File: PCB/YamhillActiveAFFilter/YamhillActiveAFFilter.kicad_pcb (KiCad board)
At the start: 2 copper layers, 50 x 50 mm, 32 parts, among them J1 Input, J2 +5V, J3 Output, U1 TL974

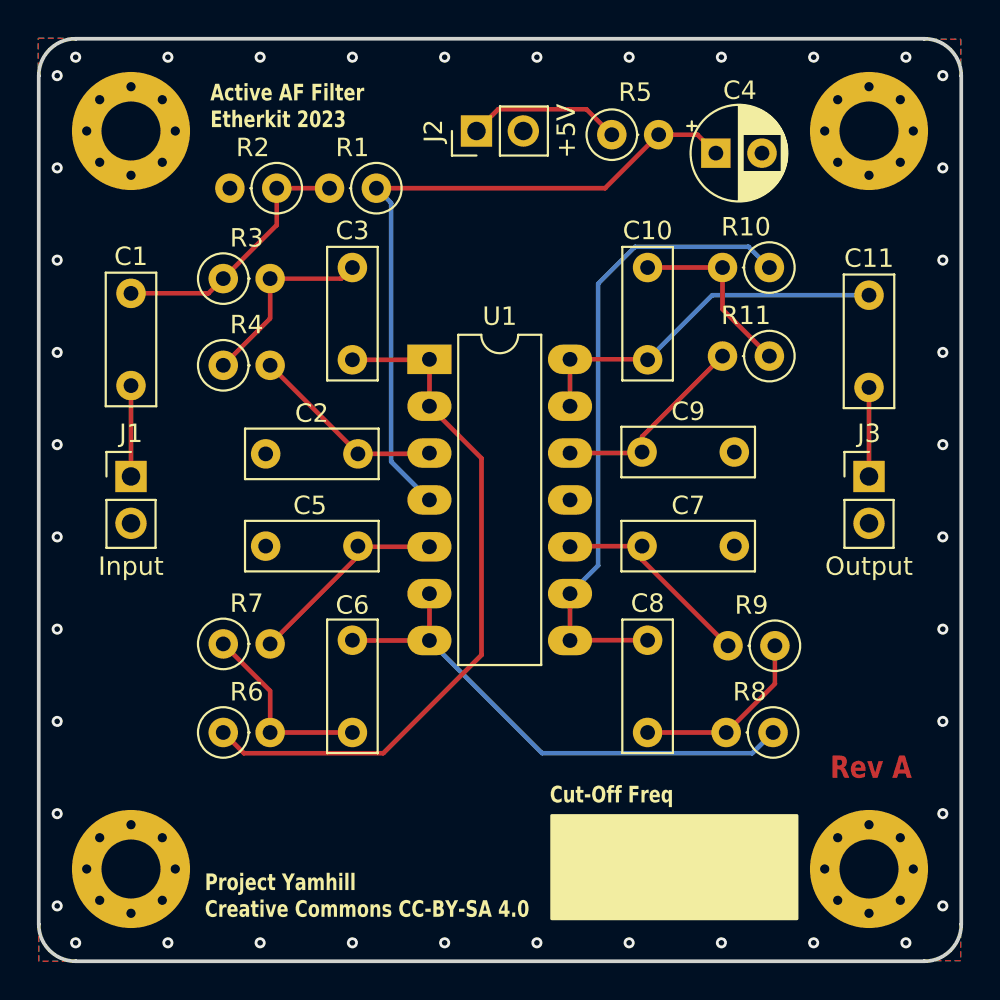
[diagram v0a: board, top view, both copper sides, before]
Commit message: AF Filter, Protoboard modules added
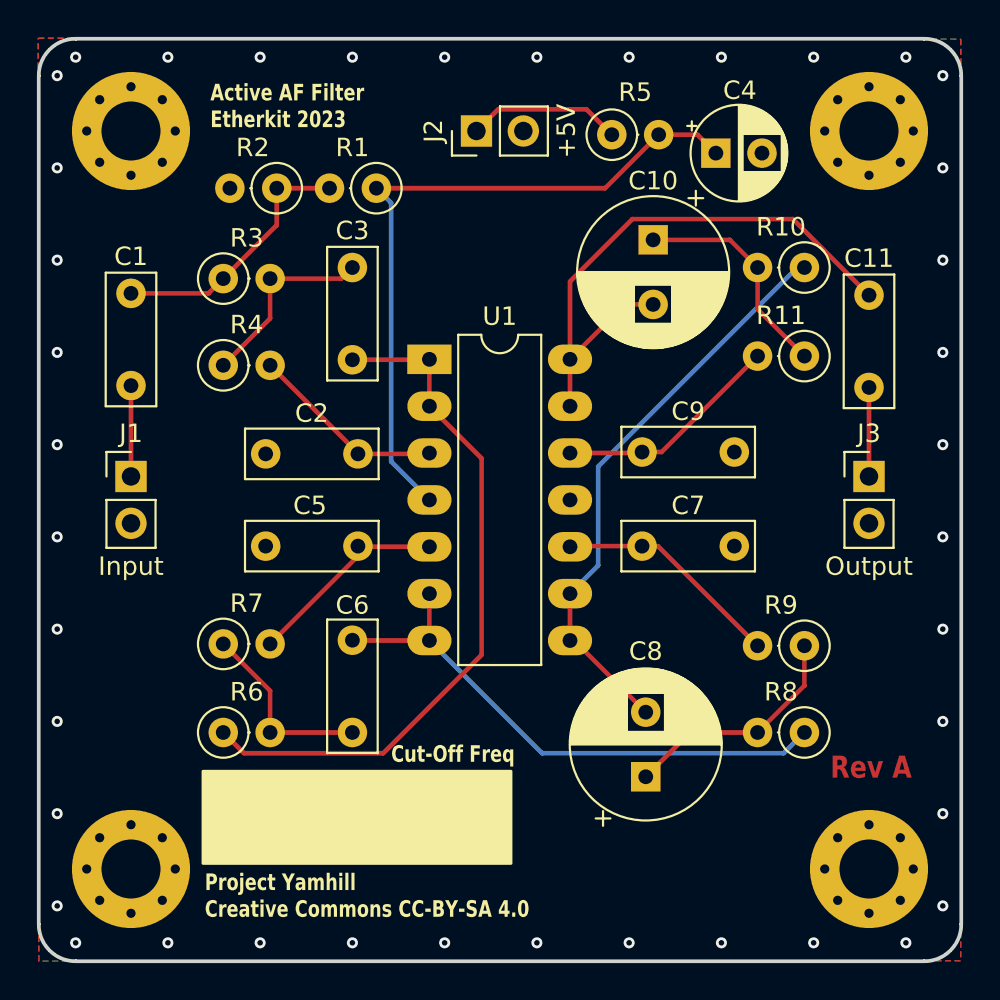
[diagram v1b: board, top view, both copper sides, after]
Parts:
- C10, C8: footprint Capacitor_THT:C_Rect_L7.0mm_W2.5mm_P5.00mm -> Capacitor_THT:CP_Radial_D8.0mm_P3.50mm
- moved C8 2.40 mm to (132.9, 90.0)
- moved R10 1.90 mm to (141.5, 62.4)
- moved R11 1.90 mm to (141.5, 67.2)
- moved R8 1.70 mm to (141.5, 87.6)
- moved R9 1.60 mm to (141.5, 82.9)
- moved C10 1.53 mm to (133.3, 60.9)
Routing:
- net Net-(U1D--): track 20.2 -> 31.8 mm
- net Net-(U1C--): track 34.8 -> 31.4 mm
- net Net-(C8-Pad1): track 10.1 -> 12.8 mm
- net Net-(C10-Pad1): track 9.91 -> 12.1 mm
- net Net-(U1B--): track 28.3 -> 30.0 mm
- net Net-(U1D-+): track 10.9 -> 12.3 mm
- net Net-(U1C-+): track 11.2 -> 12.4 mm

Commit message: Update all PCBs for first tranche order
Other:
- board text added: "Active AF Filter Etherkit 2024"
- board text removed: "Active AF Filter Etherkit 2023"
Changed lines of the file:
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@@
       (plot_on_all_layers_selection 0x0000000_00000000)
       (disableapertmacros false)
-      (usegerberextensions false)
+      (usegerberextensions true)
       (usegerberattributes true)
       (usegerberadvancedattributes true)
@@
       (plotinvisibletext false)
       (sketchpadsonfab false)
-      (subtractmaskfromsilk false)
+      (subtractmaskfromsilk true)
       (outputformat 1)
       (mirror false)
-      (drillshape 1)
+      (drillshape 0)
       (scaleselection 1)
-      (outputdirectory "")
+      (outputdirectory "fab/")
     )
   )
@@
     (effects (font (size 0.9 0.7) (thickness 0.175) bold) (justify left bottom))
   )
-  (gr_text "Active AF Filter\nEtherkit 2023" (at 109.3 54.9) (layer "F.SilkS")
+  (gr_text "Active AF Filter\nEtherkit 2024" (at 109.3 54.9) (layer "F.SilkS")
     (effects (font (size 0.9 0.7) (thickness 0.175) bold) (justify left bottom))
   )

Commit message: Front Panel Rev B revisions
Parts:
- added U2: TLV9362, EtherkitKicadLibrary:DIP-8_SOIC-8_Combo, F.Cu at (121.2, 74.9)
- G***, Ref**: moved to F.Cu
- U1: value TL974 -> TLV9362; footprint Package_DIP:DIP-14_W7.62mm_LongPads -> EtherkitKicadLibrary:DIP-8_SOIC-8_Combo
- moved U1 5.20 mm to (121.2, 62.2)
- moved C10 2.62 mm to (135.1, 62.8)
- moved Ref** 2.31 mm to (145.5, 85.1), turned to 0 degrees
- moved R10 1.73 mm to (143.2, 62.7)
- moved R11 1.73 mm to (143.2, 67.5)
- moved C11 1.48 mm to (146.4, 64.2)
- turned G*** to 0 degrees
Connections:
- C10 pad 2: Net-(U1D--) -> Net-(U2B--)
- C11 pad 1: Net-(U1D--) -> Net-(U2B--)
- C7 pad 1: Net-(U1C-+) -> Net-(U2A-+)
- C8 pad 2: Net-(U1C--) -> Net-(U2A--)
- C9 pad 1: Net-(U1D-+) -> Net-(U2B-+)
- R10 pad 1: Net-(U1C--) -> Net-(U2A--)
- R11 pad 2: Net-(U1D-+) -> Net-(U2B-+)
- R9 pad 2: Net-(U1C-+) -> Net-(U2A-+)
- U1 pad 4: Net-(U1A-V+) -> GND
- U1 pad 8: Net-(U1C--) -> Net-(U1A-V+)
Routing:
- net Net-(U2A--): track 0.00 -> 63.6 mm, vias 0 -> 1
- net Net-(U2B--): track 0.00 -> 41.7 mm, vias 0 -> 1
- net Net-(U1B--): track 30.0 -> 66.8 mm, vias 0 -> 1
- net Net-(U2A-+): track 0.00 -> 35.5 mm
- net Net-(U1D--): track 31.8 -> 0.00 mm
- net Net-(U1C--): track 31.4 -> 0.00 mm
- net Net-(U2B-+): track 0.00 -> 28.5 mm
- net Net-(U1B-+): track 11.2 -> 30.0 mm
- net Net-(U1A-V+): track 38.1 -> 53.6 mm, vias 0 -> 2
- net GND: track 0.00 -> 14.0 mm, vias 40 -> 42
- net Net-(U1C-+): track 12.4 -> 0.00 mm
- net Net-(U1D-+): track 12.3 -> 0.00 mm
- net Net-(U1A-+): track 10.7 -> 19.4 mm
- net Net-(U1A--): track 38.1 -> 42.8 mm, vias 0 -> 1
- net Net-(C10-Pad1): track 12.1 -> 11.4 mm
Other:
- board text added: "Rev B"
- board text removed: "Rev A"
